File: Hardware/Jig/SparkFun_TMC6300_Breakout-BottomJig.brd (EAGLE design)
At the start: 108.2 x 81.3 mm, 77 parts

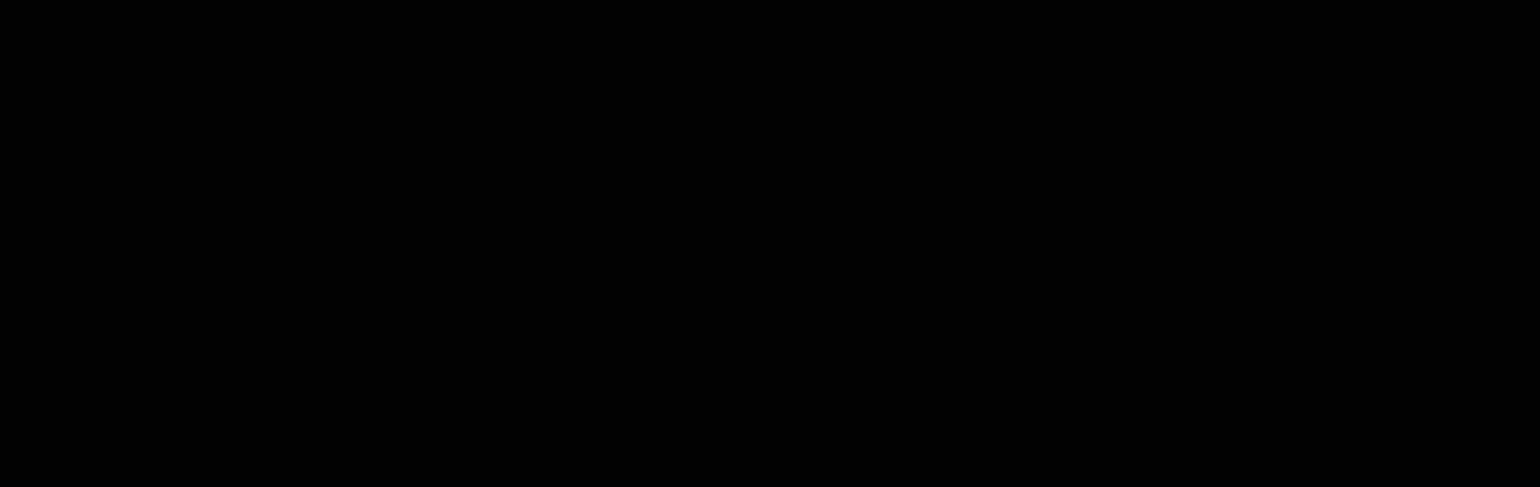
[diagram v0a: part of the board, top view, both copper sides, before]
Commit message: Add readme. Remove old files.
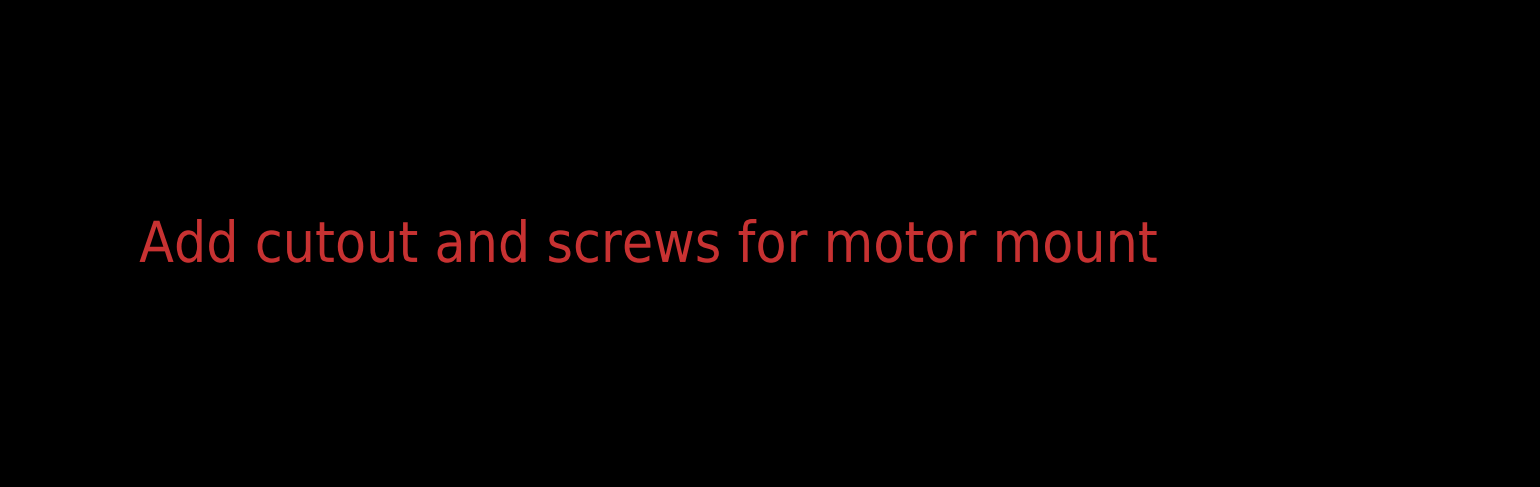
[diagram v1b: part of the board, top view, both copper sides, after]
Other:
- board text added: "Add cutout and screws for motor mount"
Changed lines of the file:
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@@
 <layer number="47" name="Measures" color="7" fill="1" visible="no" active="yes"/>
 <layer number="48" name="Document" color="7" fill="1" visible="no" active="yes"/>
-<layer number="49" name="Reference" color="7" fill="1" visible="yes" active="yes"/>
+<layer number="49" name="Reference" color="7" fill="1" visible="no" active="yes"/>
 <layer number="50" name="dxf" color="7" fill="1" visible="no" active="yes"/>
 <layer number="51" name="tDocu" color="6" fill="1" visible="yes" active="yes"/>
@@
 <wire x1="8.89" y1="24.13" x2="8.89" y2="45.72" width="0.2032" layer="51"/>
 <circle x="100" y="38" radius="16" width="0.2032" layer="21"/>
+<text x="123.19" y="45.72" size="1.778" layer="1" font="vector" ratio="15">Add cutout and screws for motor mount</text>
 </plain>
 <attributes>
